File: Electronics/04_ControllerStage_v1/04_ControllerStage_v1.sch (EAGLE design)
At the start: 43 parts, among them J1 SCREW_TERMINAL_4, J2 BARRIER_BLOCK-4PIN, J3 CONN_2X3_SMD, U1 XL4005-DEV

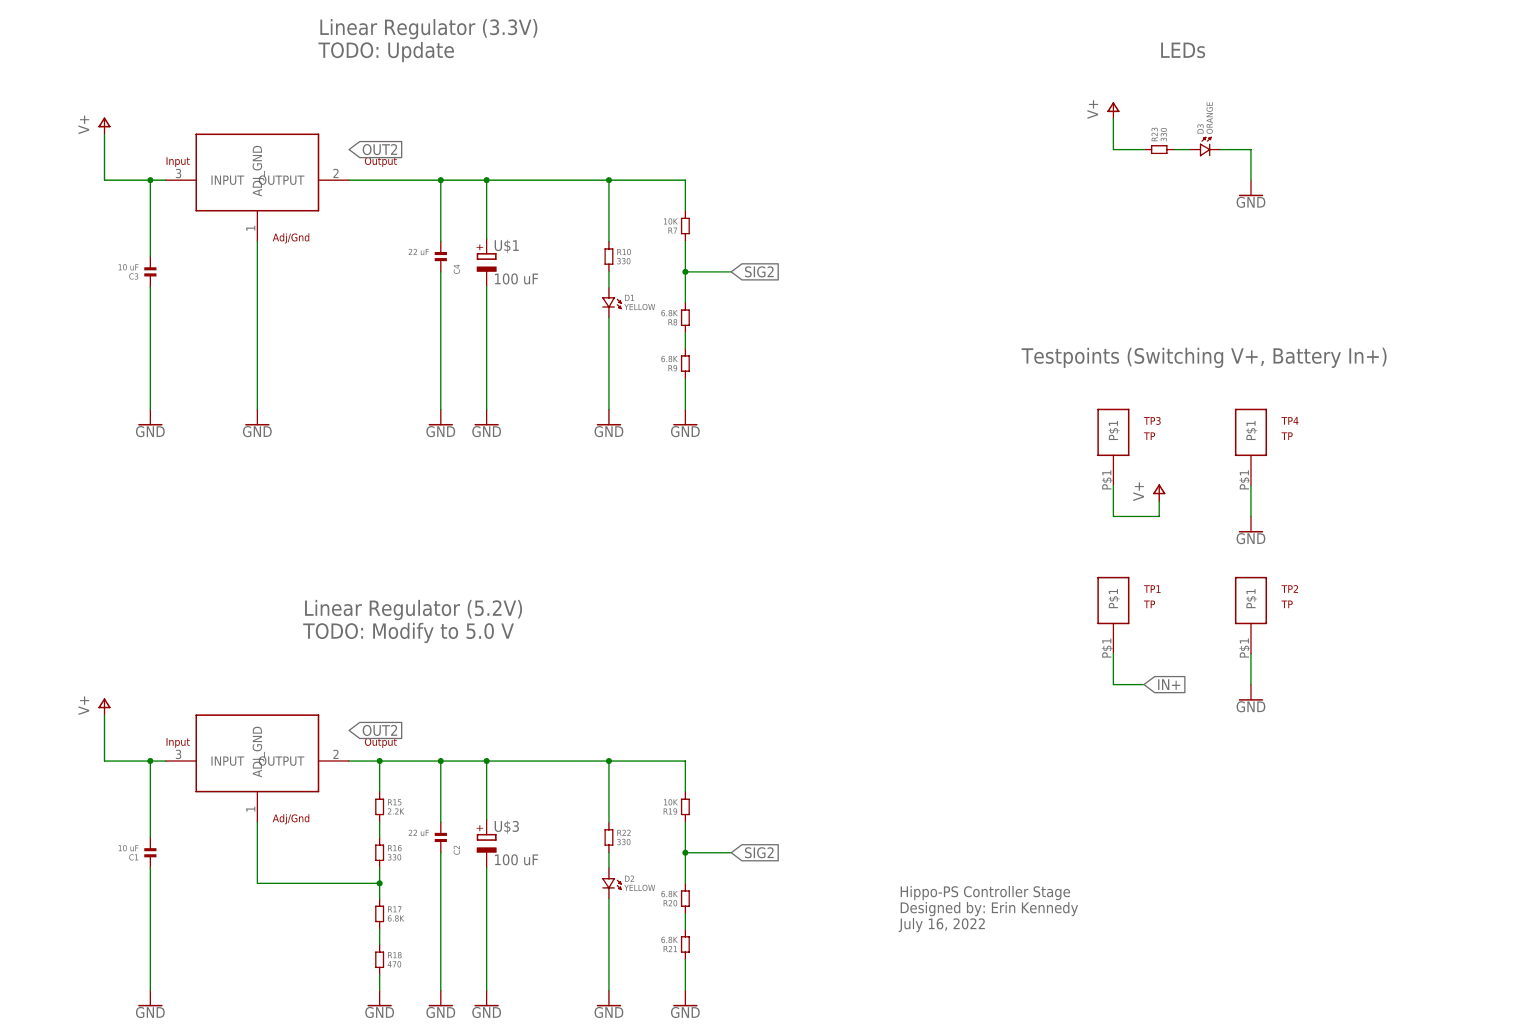
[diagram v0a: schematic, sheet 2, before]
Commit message: Components and values determined on schematic and routing started on controller stage
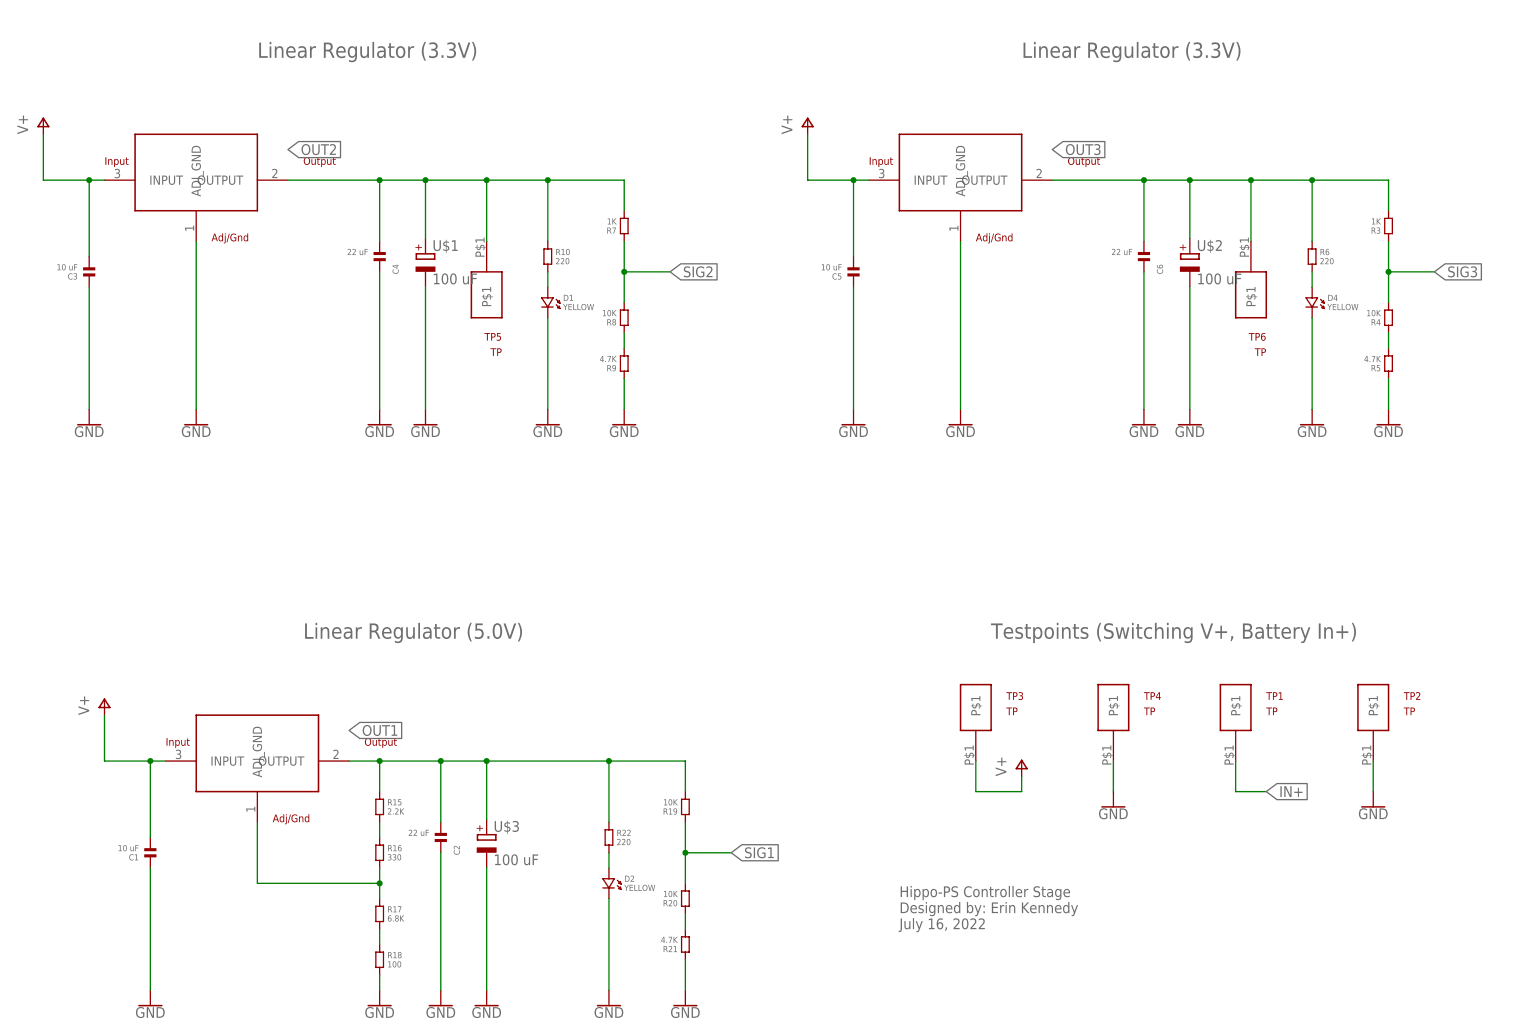
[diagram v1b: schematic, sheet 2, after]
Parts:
- removed F1: PTC, Hippo-PS:PTC
- removed TP8: TP, Hippo-PS:TP
- added C5: 10 uF, standardparts:CAPACITOR.1206
- added C6: 22 uF, standardparts:CAPACITOR.1206
- added D4: YELLOW, standardparts:LED.1206
- added R2: AZ1117CDAZ1117CD, Hippo-PS:AZ1117CDAZ1117CD
- added R3: 1K, standardparts:RESISTOR.1206
- added R4: 10K, standardparts:RESISTOR.1206
- added R5: 4.7K, standardparts:RESISTOR.1206
- added R6: 220, standardparts:RESISTOR.1206
- added TP5, TP6: TP, Hippo-PS:TP
- added U$2: 100 uF, Hippo-PS:ELECTROLYTIC_CAP
- R10, R22: value 330 -> 220
- R18: value 470 -> 100
- R20, R8: value 6.8K -> 10K
- R21, R9: value 6.8K -> 4.7K
- R7: value 10K -> 1K
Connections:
- removed net N$17: F1.1, J1.P$4, J2.P$3, TP8.P$1
- new net N$2: D4.1, R6.2
- new net N$3: R4.1, R5.2
- new net OUT3: C6.2, J1.P$3, J2.P$3, R2.OUTPUT, R3.2, R6.1, TP6.P$1, U$2.+
- new net SIG3: R3.1, R4.2
- net GND: now also C5.1, C6.1, D4.2, R2.ADJ_GND, R5.1, U$2.-
- net N$18: now also J1.P$4; no longer J1.P$3
- net OUT1: now also C2.2, F2.2, R14.OUTPUT, R15.1, R19.2, R22.1, U$3.+; no longer F1.2
- net OUT2: now also J1.P$2, J2.P$2, TP5.P$1; no longer C2.2, F2.2, R14.OUTPUT, R15.1, R19.2, R22.1, U$3.+
- net SIG1: now also R19.1, R20.2
- net SIG2: no longer R19.1, R20.2
- net V+: now also C5.2, R2.INPUT
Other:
- note added: "Linear Regulator (3.3V)"
- note added: "Linear Regulator (5.0V)"
- note removed: "Linear Regulator (3.3V) TODO: Update"
- note removed: "Linear Regulator (5.2V) TODO: Modify to 5.0 V"
- moved on the sheet: C3, C4, D1, F2, H1, H2, H3, H4, J1, J2, R10, R7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

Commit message: Finish routing controller stage electronics
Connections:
- removed net SIG_NP: J3.P$4
- net SIG1: now also J3.P$4; no longer J3.P$3
- net SIG3: now also J3.P$3
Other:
- note added: "Hippo-PD Controller Stage Designed by: Erin Kennedy July 16, 2022"
- note removed: "Hippo-PS Controller Stage Designed by: Erin Kennedy July 16, 2022"
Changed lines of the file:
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@@
 <text x="81.28" y="121.92" size="2.54" layer="95">Output of Regulators</text>
 <text x="180.34" y="66.04" size="2.54" layer="95">Brass Standoffs</text>
-<text x="149.86" y="25.4" size="1.778" layer="95">Hippo-PS Controller Stage
+<text x="149.86" y="25.4" size="1.778" layer="95">Hippo-PD Controller Stage
 Designed by: Erin Kennedy
 July 16, 2022</text>
@@
 </segment>
 </net>
-<net name="SIG_NP" class="0">
+<net name="SIG1" class="0">
 <segment>
 <pinref part="J3" gate="G$1" pin="P$4"/>
@@
 </segment>
 </net>
-<net name="SIG1" class="0">
-<segment>
-<pinref part="J3" gate="G$1" pin="P$3"/>
-<wire x1="200.66" y1="147.32" x2="205.74" y2="147.32" width="0.1524" layer="91"/>
-<label x="205.74" y="147.32" size="1.778" layer="95" xref="yes"/>
-</segment>
-</net>
 <net name="SIG2" class="0">
 <segment>
@@
 </segment>
 </net>
+<net name="SIG3" class="0">
+<segment>
+<pinref part="J3" gate="G$1" pin="P$3"/>
+<wire x1="200.66" y1="147.32" x2="205.74" y2="147.32" width="0.1524" layer="91"/>
+<label x="205.74" y="147.32" size="1.778" layer="95" xref="yes"/>
+</segment>
+</net>
 </nets>
 </sheet>
@@
 <plain>
 <text x="50.8" y="73.66" size="2.54" layer="95">Linear Regulator (5.0V)</text>
-<text x="149.86" y="25.4" size="1.778" layer="95">Hippo-PS Controller Stage
+<text x="149.86" y="25.4" size="1.778" layer="95">Hippo-PD Controller Stage
 Designed by: Erin Kennedy
 July 16, 2022</text>
